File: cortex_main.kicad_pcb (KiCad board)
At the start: 2 copper layers, 119.4 x 119.4 mm, 12 parts, among them P1 CONN_01X05, P2 CONN_02X04, P3 CONN_01X02, P4 CONN_01X04, P5 CONN_01X02, U1 socket_leon_x3_dil64, U2 socket_pololu_24v12, U3 socket_pololu_24v12, U4 socket_lm2596_mod, U5 socket_ams1117-3V3_mod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

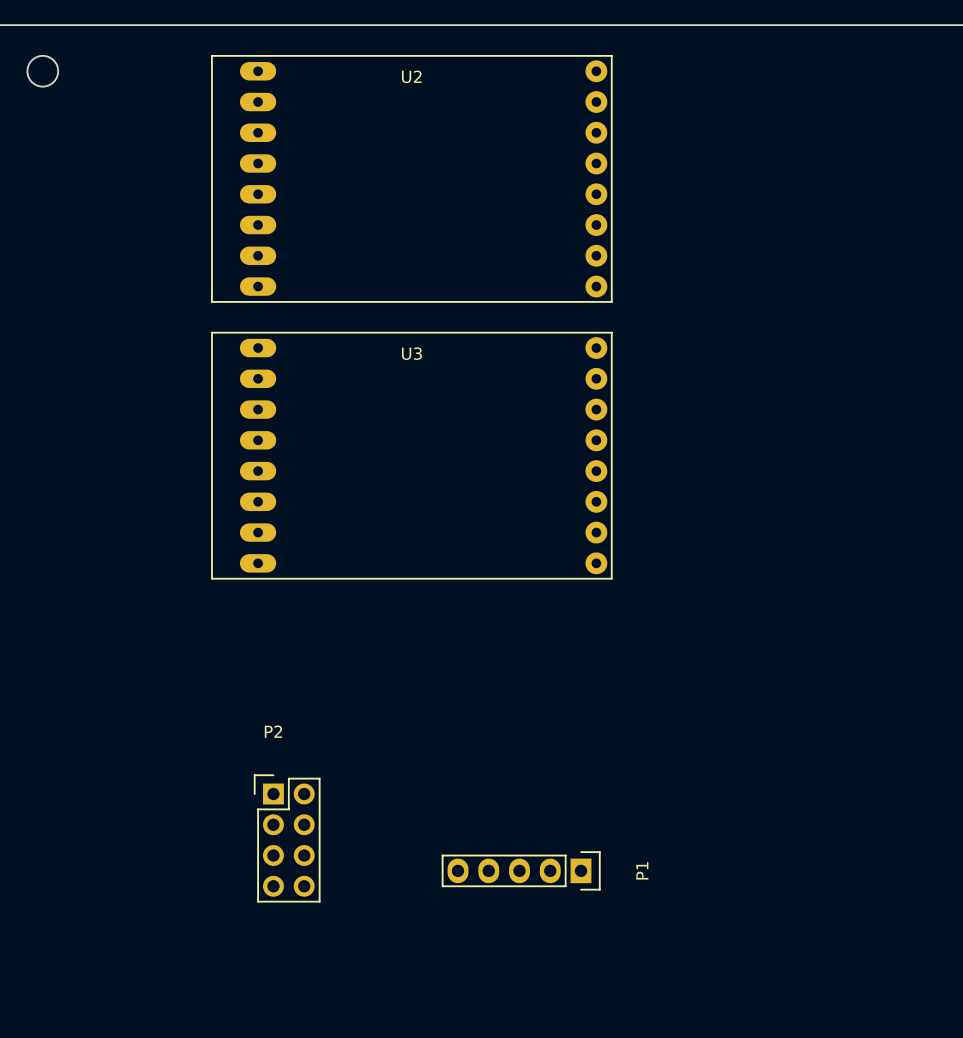
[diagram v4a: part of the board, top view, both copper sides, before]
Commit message: cortex: pcb: place RGB connectors
Signed-off-by: Yannick Gicquel <ygicquel@gmail.com>
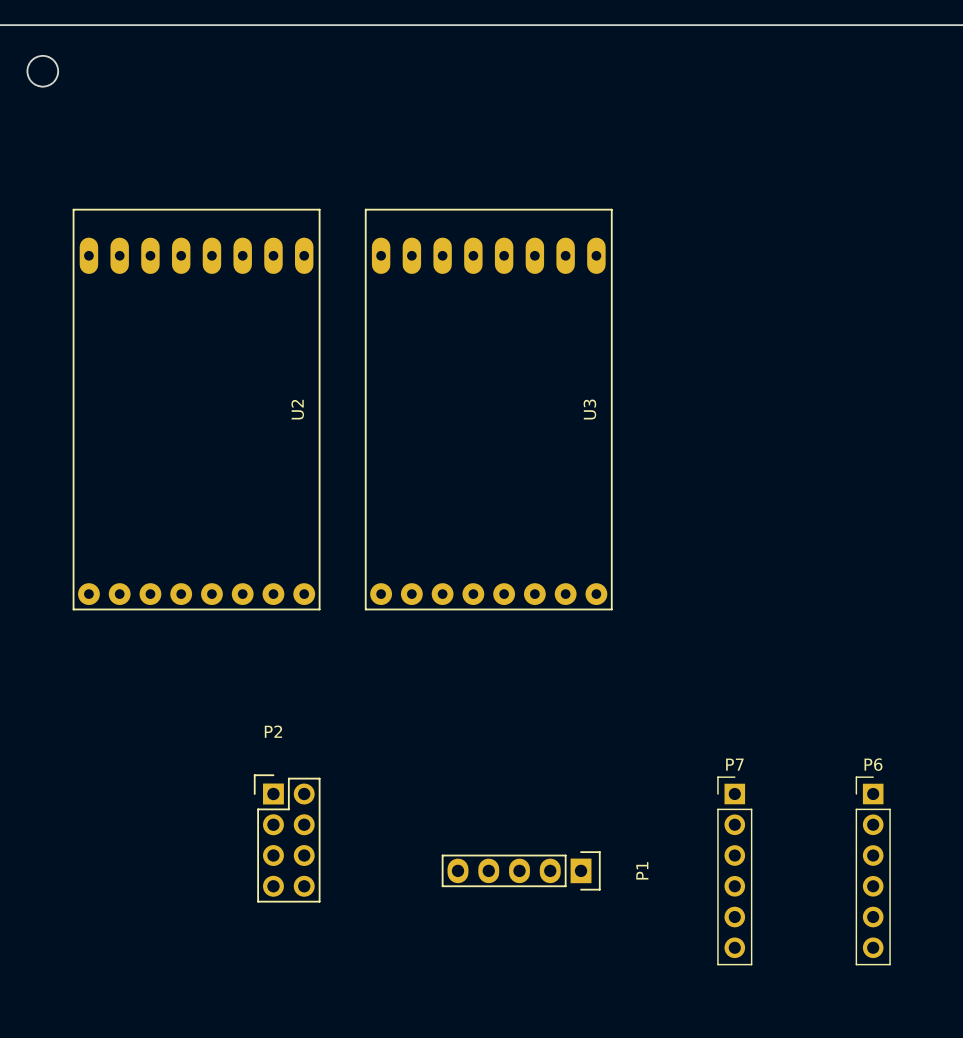
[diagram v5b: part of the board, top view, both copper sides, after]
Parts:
- added P6: CONN_01X06, Pin_Headers:Pin_Header_Straight_1x06_Pitch2.54mm, F.Cu at (108.0, 113.0)
- added P7: CONN_01X06, Pin_Headers:Pin_Header_Straight_1x06_Pitch2.54mm, F.Cu at (96.5, 113.0)
- moved U2 26.1 mm to (52.1, 81.3), turned to 270 degrees
- moved U3 7.41 mm to (76.2, 81.3), turned to 270 degrees
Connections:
- net /Sheet_Connectors/SCL renamed /Sheet_Connectors/SCL_C
- net /Sheet_Connectors/SDA renamed /Sheet_Connectors/SDA_C
- U1 pad 26: Net-(U1-Pad26) -> /Sheet_Connectors/SDA_D
- U1 pad 27: Net-(U1-Pad27) -> /Sheet_Connectors/SCL_D
- U1 pad 28: Net-(U1-Pad28) -> /Sheet_Connectors/RGB_LEDEN_L
- U1 pad 29: Net-(U1-Pad29) -> /Sheet_Connectors/RGB_LEDEN_R

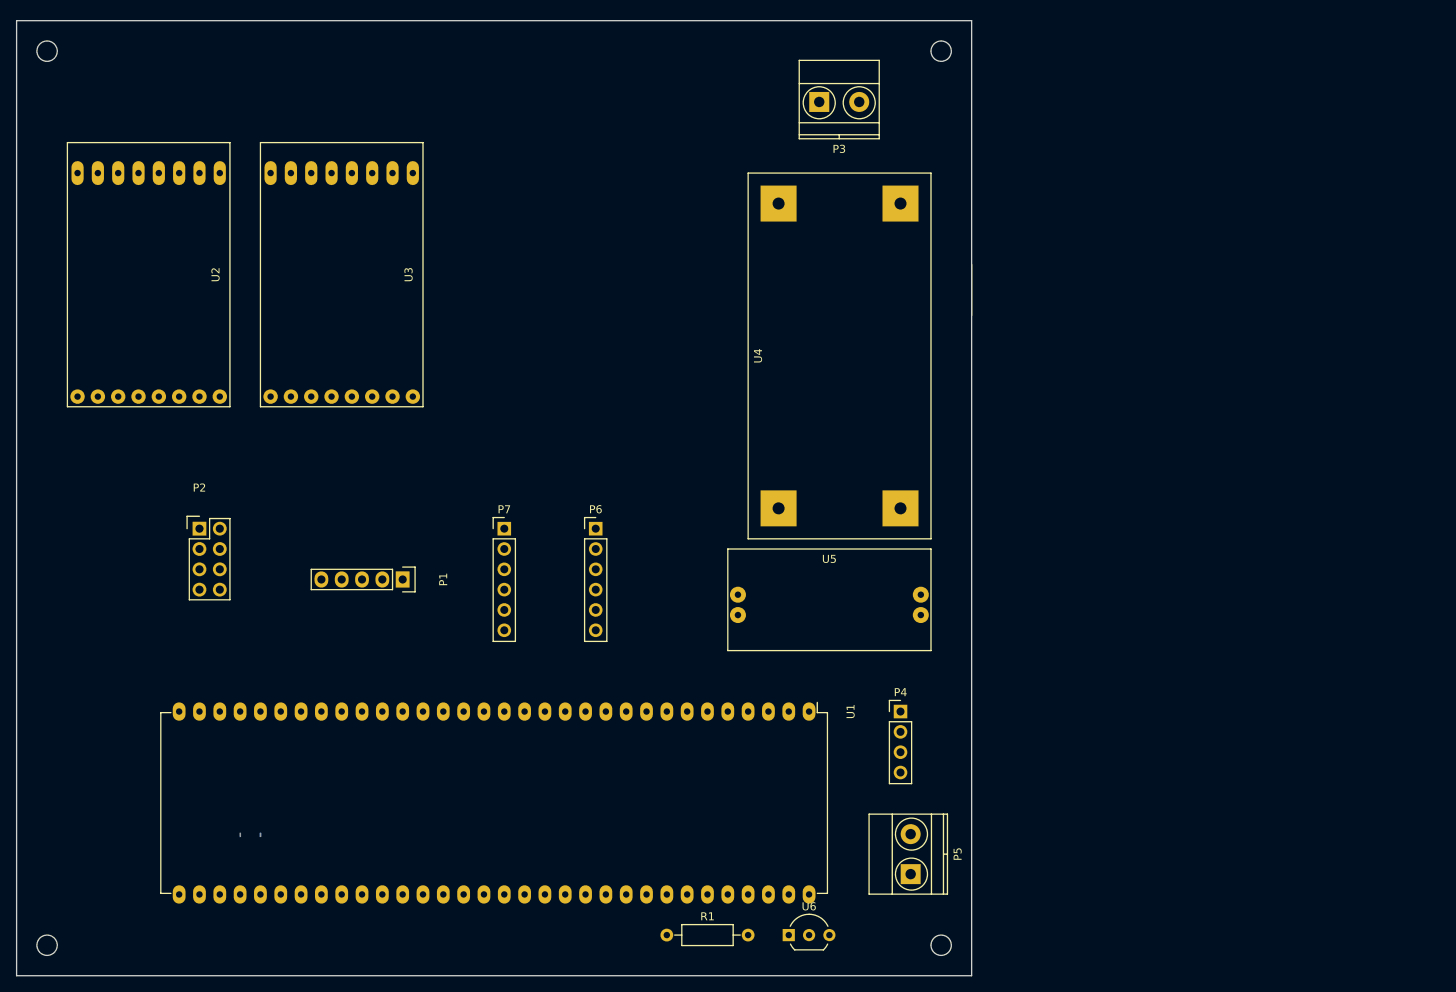
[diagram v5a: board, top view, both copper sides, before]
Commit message: cortex: add Sharp IR sensors connectors
on schematic & pcb.

Signed-off-by: Yannick Gicquel <ygicquel@gmail.com>
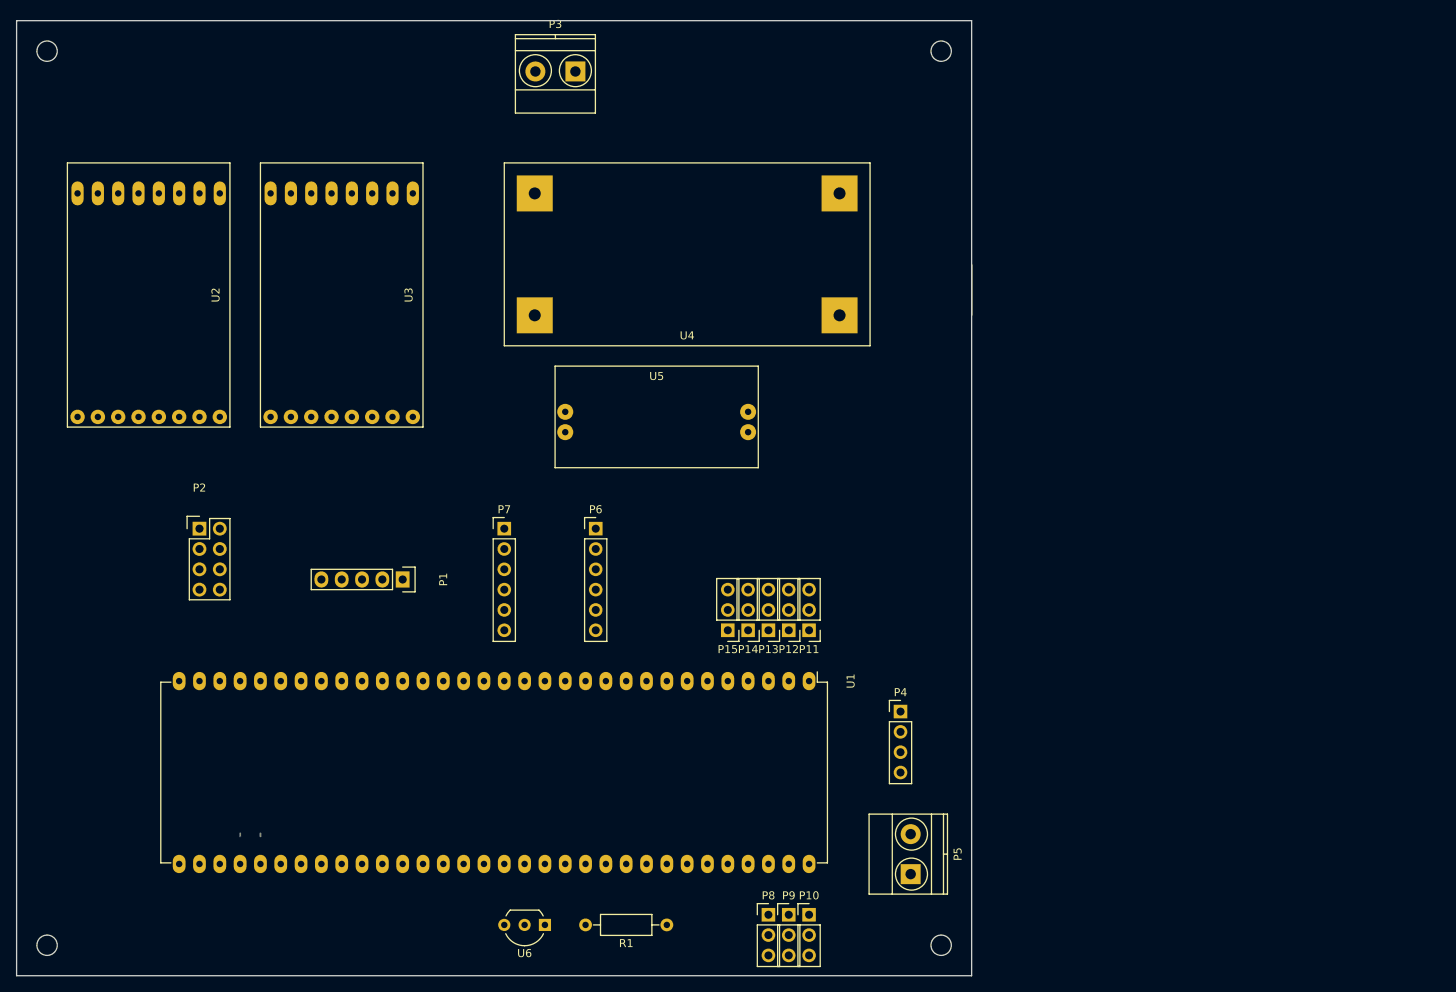
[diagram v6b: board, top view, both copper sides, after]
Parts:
- added P10: CONN_01X03, Pin_Headers:Pin_Header_Straight_1x03_Pitch2.54mm, F.Cu at (134.6, 161.3)
- added P11: CONN_01X03, Pin_Headers:Pin_Header_Straight_1x03_Pitch2.54mm, F.Cu at (134.6, 125.7)
- added P12: CONN_01X03, Pin_Headers:Pin_Header_Straight_1x03_Pitch2.54mm, F.Cu at (132.1, 125.7)
- added P13: CONN_01X03, Pin_Headers:Pin_Header_Straight_1x03_Pitch2.54mm, F.Cu at (129.5, 125.7)
- added P14: CONN_01X03, Pin_Headers:Pin_Header_Straight_1x03_Pitch2.54mm, F.Cu at (127.0, 125.7)
- added P15: CONN_01X03, Pin_Headers:Pin_Header_Straight_1x03_Pitch2.54mm, F.Cu at (124.5, 125.7)
- added P8: CONN_01X03, Pin_Headers:Pin_Header_Straight_1x03_Pitch2.54mm, F.Cu at (129.5, 161.3)
- added P9: CONN_01X03, Pin_Headers:Pin_Header_Straight_1x03_Pitch2.54mm, F.Cu at (132.1, 161.3)
- moved U5 31.4 mm to (115.6, 99.1)
- moved P3 30.7 mm to (105.4, 55.9), turned to 180 degrees
- moved U6 30.5 mm to (101.6, 162.6), turned to 180 degrees
- moved U4 22.9 mm to (119.4, 78.7), turned to 0 degrees
- moved U1 3.81 mm to (134.6, 132.1)
- moved U2 2.54 mm to (52.1, 83.8)
- moved U3 2.54 mm to (76.2, 83.8)
- moved R1 1.27 mm to (116.8, 162.6), turned to 180 degrees
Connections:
- U1 pad 1: Net-(U1-Pad1) -> IR_VIN_3
- U1 pad 2: Net-(U1-Pad2) -> IR_VIN_4
- U1 pad 3: Net-(U1-Pad3) -> IR_VIN_5
- U1 pad 4: Net-(U1-Pad4) -> IR_VIN_6
- U1 pad 5: Net-(U1-Pad5) -> IR_VIN_7
- U1 pad 62: Net-(U1-Pad62) -> IR_VIN_0
- U1 pad 63: Net-(U1-Pad63) -> IR_VIN_1
- U1 pad 64: Net-(U1-Pad64) -> IR_VIN_2

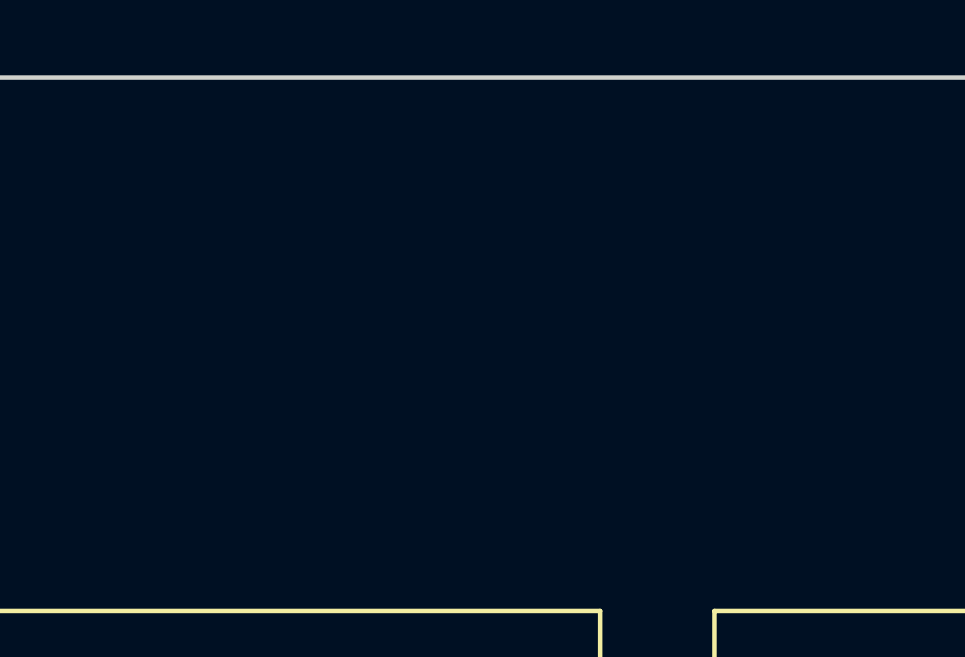
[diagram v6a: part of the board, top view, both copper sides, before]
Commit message: cortex: add Motors connectors
on sch & pcb.

Signed-off-by: Yannick Gicquel <ygicquel@gmail.com>
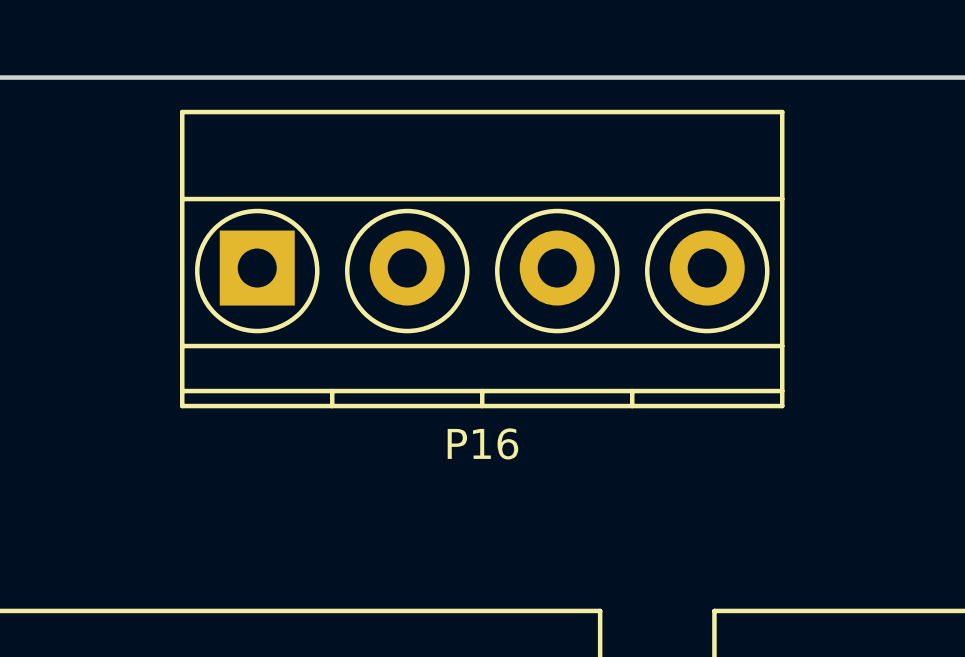
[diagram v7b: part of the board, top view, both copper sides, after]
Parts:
- added P16: CONN_01X04, Terminal_Blocks:TerminalBlock_Pheonix_MKDS1.5-4pol, F.Cu at (50.8, 55.9)
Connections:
- net /Sheet_Motors/OUTA_L renamed OUTA_L
- net /Sheet_Motors/OUTA_R renamed OUTA_R
- net /Sheet_Motors/OUTB_L renamed OUTB_L
- net /Sheet_Motors/OUTB_R renamed OUTB_R

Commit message: cortex: pcb: start output layout
Signed-off-by: Yannick Gicquel <ygicquel@gmail.com>
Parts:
- added P17: CONN_01X02, Terminal_Blocks:TerminalBlock_Pheonix_MKDS1.5-2pol, F.Cu at (53.3, 58.4)
- P16: value CONN_01X04 -> CONN_01X02; footprint Terminal_Blocks:TerminalBlock_Pheonix_MKDS1.5-4pol -> Terminal_Blocks:TerminalBlock_Pheonix_MKDS1.5-2pol
- moved P2 49.9 mm to (71.1, 161.3), turned to 270 degrees
- moved P16 28.1 mm to (78.7, 58.4), turned to 180 degrees
- moved P7 27.9 mm to (68.6, 113.0)
- moved P6 14.0 mm to (94.0, 113.0)
- moved U4 12.6 mm to (128.3, 69.8)
- moved U5 9.16 mm to (120.7, 91.4)
- moved P3 6.84 mm to (99.1, 58.4)
- moved U6 5.08 mm to (106.7, 162.6)
- moved P1 4.02 mm to (85.1, 115.6), turned to 0 degrees
- moved R1 2.54 mm to (119.4, 162.6)
- moved U2 1.27 mm to (50.8, 83.8)
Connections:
- P16 pad 1: OUTB_L -> OUTA_R
- P16 pad 2: OUTA_L -> OUTB_R
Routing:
- net +24V: track 0.00 -> 26.5 mm
- net (no net): track 0.70 -> 0.00 mm
- added copper zone on B.Cu, net +24V
- added copper zone on B.Cu, net GND
- added copper zone on B.Cu, net OUTA_L
- added copper zone on B.Cu, net OUTA_R
- added copper zone on B.Cu, net OUTB_L
- added copper zone on B.Cu, net OUTB_R
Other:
- net class BigPower added: clearance 0.2, trace_width 3, via_dia 0.6, via_drill 0.4
